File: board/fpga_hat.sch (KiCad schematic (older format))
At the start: 78 parts, among them J1 2x20, J2 AudioJack3, J3 Conn_02x06_Top_Bottom, J4 Conn_02x06_Top_Bottom, J5 Conn_02x06_Top_Bottom, SW1 SW_Push, SW2 SW_Push, SW3 SW_Push, SW4 SW_Push, SW5 SW_Push, SW6 SW_Push, SW7 SW_Push, SW8 SW_Push, SW9 SW_Push, U1 iCE40-HX8k-BG121, U2 CAT24C32WI, U3 MIC23050-4YML, U4 74LVC2G07, U5 DSC60XX, U6 NCP115ASN330T, U7 W25X40CL, U8 IS61WV25616

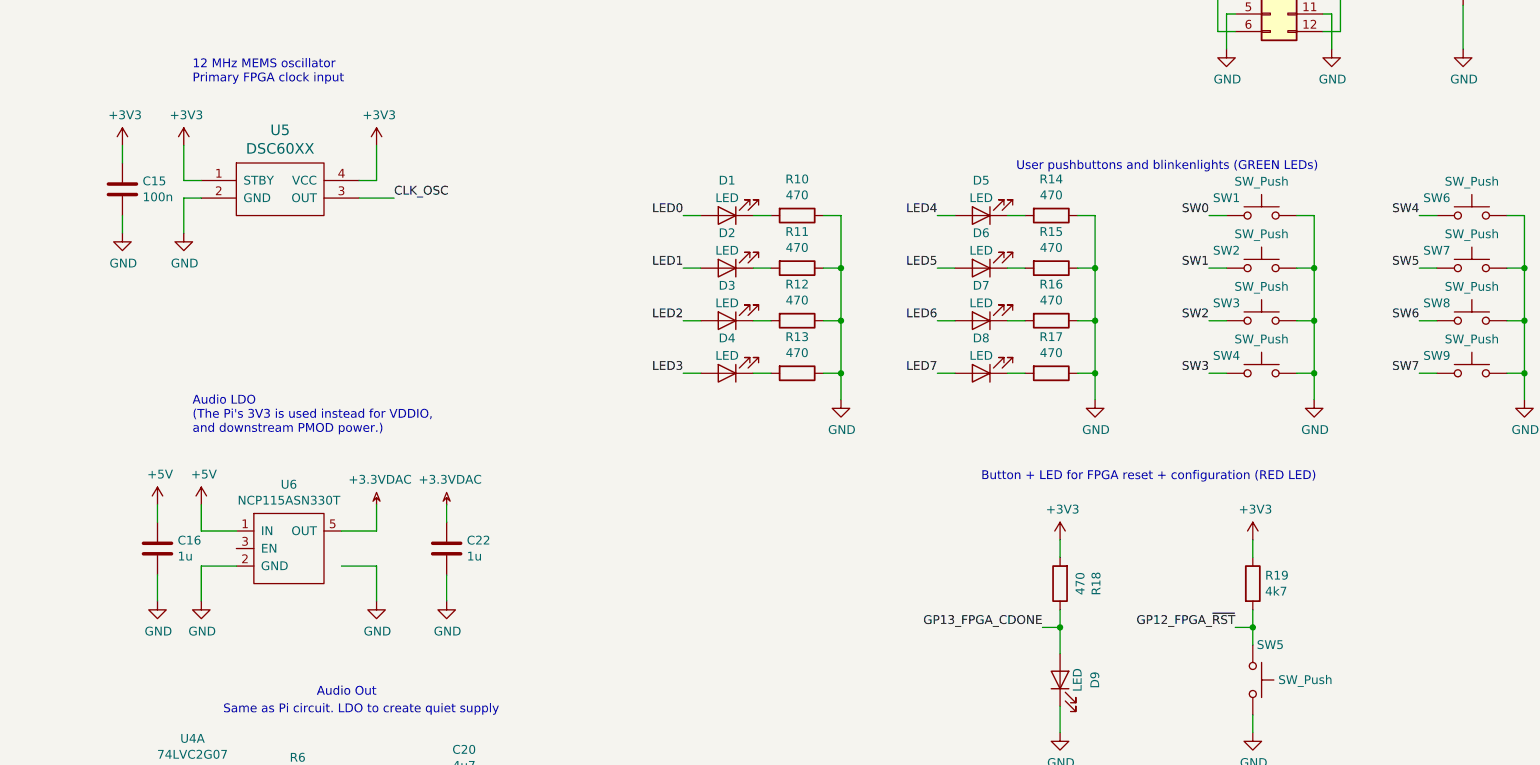
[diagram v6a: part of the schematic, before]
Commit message: Add footprints for FPGA, SRAM, SMPS. Do some footprint association.
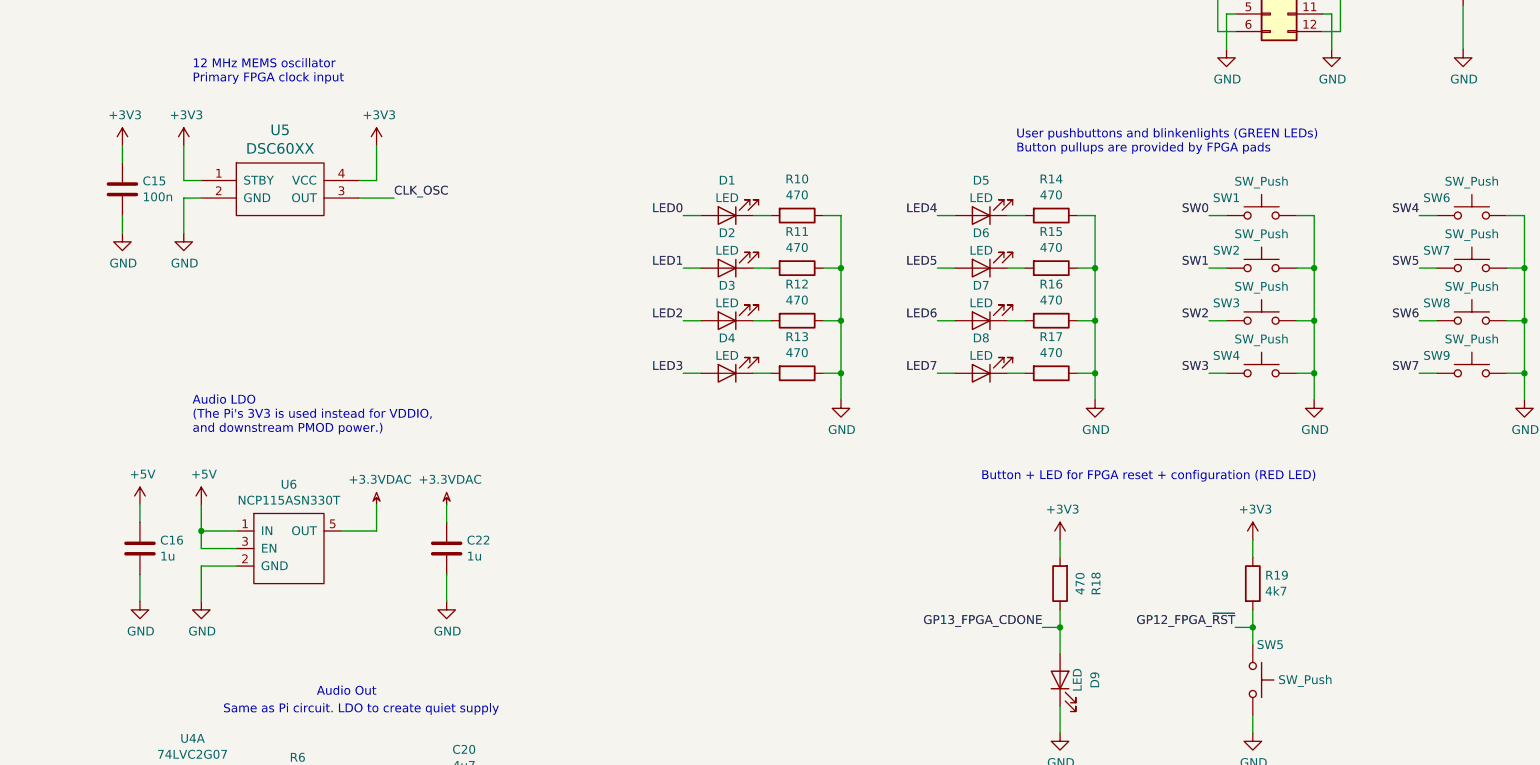
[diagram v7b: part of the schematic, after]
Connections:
- net +5V: now also U6.3 (EN)
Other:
- note added: "User pushbuttons and blinkenlights (GREEN LEDs)\nButton pullups are provided by FPGA pads"
- note removed: "User pushbuttons and blinkenlights (GREEN LEDs)"
- moved on the sheet: C16
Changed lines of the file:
@@
 	1    0    0    -1
 $EndComp
-$Comp
-L power:GND #PWR060
-U 1 1 5D1B5A98
-P 9250 8100
-F 0 "#PWR060" H 9250 7850 50  0001 C CNN
-F 1 "GND" H 9255 7927 50  0000 C CNN
-F 2 "" H 9250 8100 50  0001 C CNN
-F 3 "" H 9250 8100 50  0001 C CNN
-	1    9250 8100
-	1    0    0    -1
-$EndComp
-Wire Wire Line
-	9050 7900 9250 7900
-Wire Wire Line
-	9250 7900 9250 8100
 Wire Wire Line
 	9050 7700 9250 7700
@@
 L Device:C C16
 U 1 1 5D1BD1CA
-P 8000 7800
-F 0 "C16" H 8115 7846 50  0000 L CNN
-F 1 "1u" H 8115 7755 50  0000 L CNN
-F 2 "" H 8038 7650 50  0001 C CNN
-F 3 "~" H 8000 7800 50  0001 C CNN
-	1    8000 7800
+P 7900 7800
+F 0 "C16" H 8015 7846 50  0000 L CNN
+F 1 "1u" H 8015 7755 50  0000 L CNN
+F 2 "" H 7938 7650 50  0001 C CNN
+F 3 "~" H 7900 7800 50  0001 C CNN
+	1    7900 7800
 	1    0    0    -1
 $EndComp
@@
 L power:+5V #PWR046
 U 1 1 5D1BD21A
-P 8000 7550
-F 0 "#PWR046" H 8000 7400 50  0001 C CNN
-F 1 "+5V" H 8015 7723 50  0000 C CNN
-F 2 "" H 8000 7550 50  0001 C CNN
-F 3 "" H 8000 7550 50  0001 C CNN
-	1    8000 7550
+P 7900 7550
+F 0 "#PWR046" H 7900 7400 50  0001 C CNN
+F 1 "+5V" H 7915 7723 50  0000 C CNN
+F 2 "" H 7900 7550 50  0001 C CNN
+F 3 "" H 7900 7550 50  0001 C CNN
+	1    7900 7550
 	1    0    0    -1
 $EndComp
@@
 L power:GND #PWR047
 U 1 1 5D1BD25B
-P 8000 8100
-F 0 "#PWR047" H 8000 7850 50  0001 C CNN
-F 1 "GND" H 8005 7927 50  0000 C CNN
-F 2 "" H 8000 8100 50  0001 C CNN
-F 3 "" H 8000 8100 50  0001 C CNN
-	1    8000 8100
-	1    0    0    -1
-$EndComp
-Wire Wire Line
-	8000 7650 8000 7550
-Wire Wire Line
-	8000 7950 8000 8100
+P 7900 8100
+F 0 "#PWR047" H 7900 7850 50  0001 C CNN
+F 1 "GND" H 7905 7927 50  0000 C CNN
+F 2 "" H 7900 8100 50  0001 C CNN
+F 3 "" H 7900 8100 50  0001 C CNN
+	1    7900 8100
+	1    0    0    -1
+$EndComp
+Wire Wire Line
+	7900 7650 7900 7550
+Wire Wire Line
+	7900 7950 7900 8100
 $Comp
 L power:+3.3VDAC #PWR064
@@
 Text Label 15200 6800 2    50   ~ 0
 SW7
-Text Notes 12900 5650 0    50   ~ 0
-User pushbuttons and blinkenlights (GREEN LEDs)
+Text Notes 12900 5550 0    50   ~ 0
+User pushbuttons and blinkenlights (GREEN LEDs)\nButton pullups are provided by FPGA pads
 Text Notes 8200 7150 0    50   ~ 0
 Audio LDO\n(The Pi's 3V3 is used instead for VDDIO,\nand downstream PMOD power.)
@@
 Wire Wire Line
 	1350 1950 1350 2000
+Wire Wire Line
+	8450 7800 8250 7800
+Wire Wire Line
+	8250 7800 8250 7700
+Connection ~ 8250 7700
 $EndSCHEMATC

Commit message: More footprints
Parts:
- C1, C10, C11, C13, C15, C17, C18, C19, C3, C5, C6, C7, C8, C9: footprint (none) -> Capacitor_SMD:C_0402_1005Metric
- C12, C14, C16, C2, C20, C21, C22, C23, C24, C25, C4: footprint (none) -> Capacitor_SMD:C_0603_1608Metric
- D1, D2, D3, D4, D5, D6, D7, D8, D9: footprint (none) -> LED_SMD:LED_0805_2012Metric
- J1: footprint (none) -> Connector_PinHeader_2.54mm:PinHeader_2x20_P2.54mm_Vertical
- J3, J4, J5: footprint (none) -> Connector_PinSocket_2.54mm:PinSocket_2x06_P2.54mm_Horizontal
- JP1: footprint (none) -> fpga_hat:SOLDER_JUMP
- L1: footprint (none) -> Inductor_SMD:L_0805_2012Metric
- R1, R10, R11, R12, R13, R14, R15, R16, R17, R18, R19, R2, R3, R4, R5, R6, R7, R8, R9: footprint (none) -> Resistor_SMD:R_0402_1005Metric
- SW1, SW2, SW3, SW4, SW5, SW6, SW7, SW8, SW9: footprint (none) -> Button_Switch_SMD:SW_SPST_EVQQ2
- U1: footprint (none) -> fpga_hat:BGA-121_11x11_9.0x9.0mm
- U2: footprint (none) -> Package_SO:TSSOP-8_4.4x3mm_P0.65mm
- U3: footprint (none) -> Package_TO_SOT_SMD:SOT-23-5_HandSoldering
- U6: footprint (none) -> fpga_hat:DFN8_2x2_0.5mm
- U7: footprint (none) -> Package_SO:SOIC-8_3.9x4.9mm_P1.27mm
- U8: footprint (none) -> fpga_hat:BGA-48_6x8_6.0x8.0mm
